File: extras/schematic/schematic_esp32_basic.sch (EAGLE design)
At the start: 23 parts, among them U1 SI4735-D60-GU

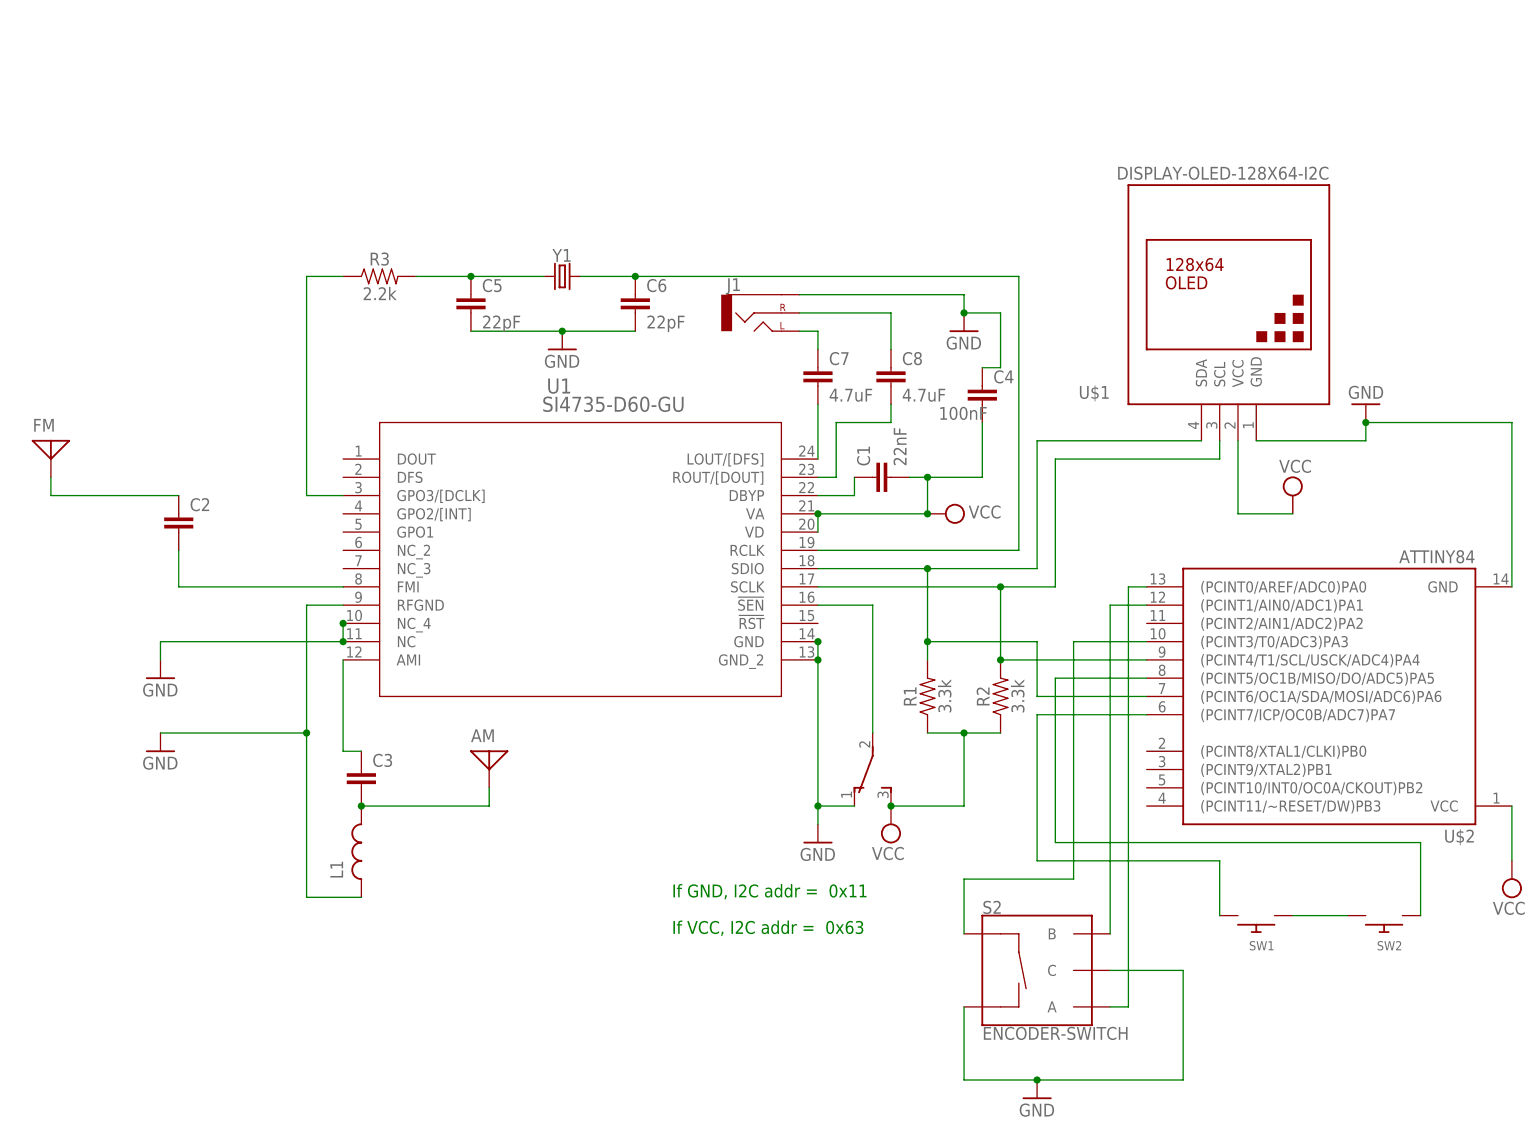
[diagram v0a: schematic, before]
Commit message: SI473X Arduino Library
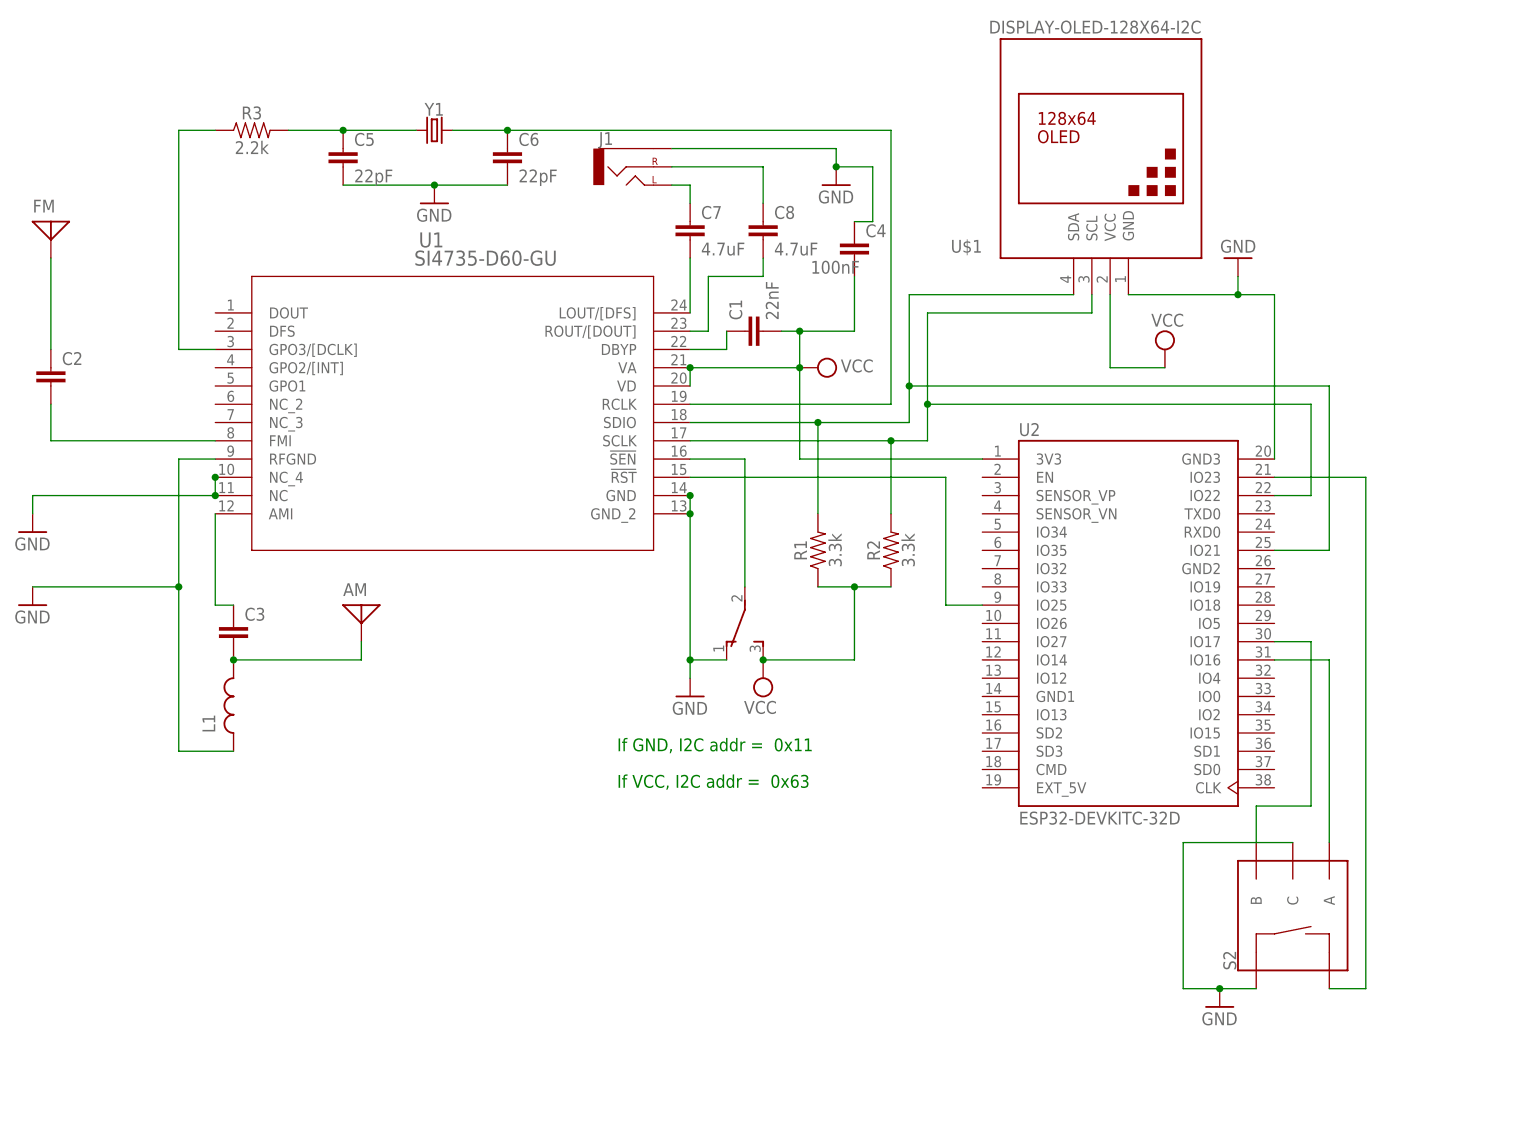
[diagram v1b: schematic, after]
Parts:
- removed SW1, SW2: (no value), adafruit:SWITCH_PUSHBUTTONEVQ-PE
- removed U$2: ATTINY84, SparkFun-IC-Microcontroller:ATTINY84
- added U2: ESP32-DEVKITC-32D, ESP32-DEVKITC-32D:ESP32-DEVKITC-32D
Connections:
- removed net N$1 (its old number): S2.B, U$2.(PCINT1/AIN0/ADC1)PA1
- removed net N$18: SW1.P$1, SW2.P$2
- removed net N$19: SW1.P$2, U$2.(PCINT7/ICP/OC0B/ADC7)PA7
- new net N$14: S2.A, U2.IO16
- net GND: now also S2.SW+, U2.GND3; no longer S2.SW-, U$2.GND
- net N$15: now also U2.IO21; no longer U$2.(PCINT6/OC1A/SDA/MOSI/ADC6)PA6
- net N$16: now also S2.B, U2.IO17; no longer S2.A, U$2.(PCINT0/AREF/ADC0)PA0
- net N$17: now also U1.!RST, U2.IO25; no longer S2.SW+, U$2.(PCINT3/T0/ADC3)PA3
- net N$20: now also S2.SW-, U2.IO23; no longer SW2.P$1, U$2.(PCINT5/OC1B/MISO/DO/ADC5)PA5
- net SDA: now also U2.IO22; no longer U$2.(PCINT4/T1/SCL/USCK/ADC4)PA4
- net VCC: now also U2.3V3; no longer U$2.VCC
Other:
- moved on the sheet: AM, C1, C2, C3, C4, C5, C6, C7, C8, FM, J1, L1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
